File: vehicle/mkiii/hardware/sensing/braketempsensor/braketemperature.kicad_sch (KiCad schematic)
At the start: 15 parts, among them J1 J_PCIe_x1, J2 J_Programming_Pin_Header, U1 MCP2561-E_SN, U2 STM32G441KBT6, Y1 X_16MHz_18pF

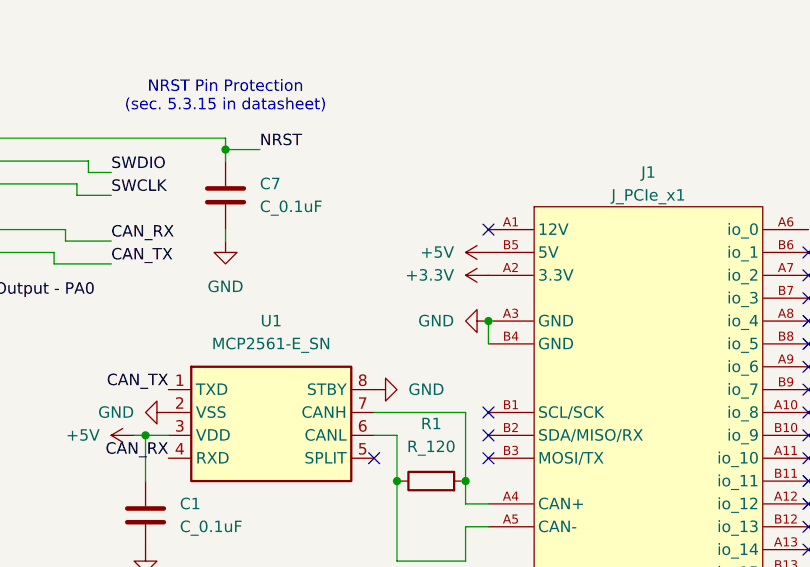
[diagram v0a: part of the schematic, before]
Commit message: first final draft of brake temp sensor, schematic and pcb layout first completion
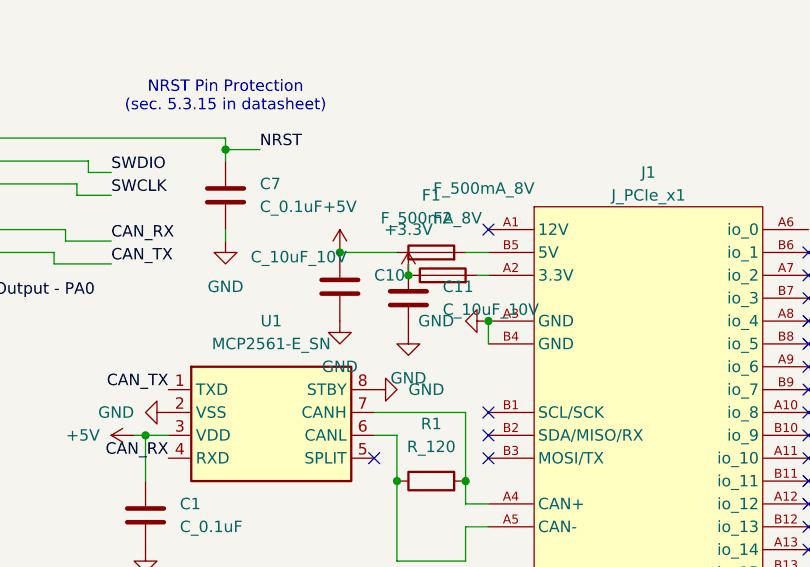
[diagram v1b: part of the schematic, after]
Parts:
- added C10, C11: C_10uF_10V, OEM:C_0603_1608Metric, symbol OEM:C_10uF_10V_0603
- added F1, F2: F_500mA_8V, OEM:Fuse_1206_3216Metric, symbol OEM:F_500mA_8V_1206
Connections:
- net +3.3V: now also C11.1, F2.1; no longer J1.A2 (3.3V)
- net +5V: now also C10.1, F1.1; no longer J1.B5 (5V)
- net GND: now also C10.2, C11.2
- new net: F1.2, J1.B5 (5V)
- new net: F2.2, J1.A2 (3.3V)

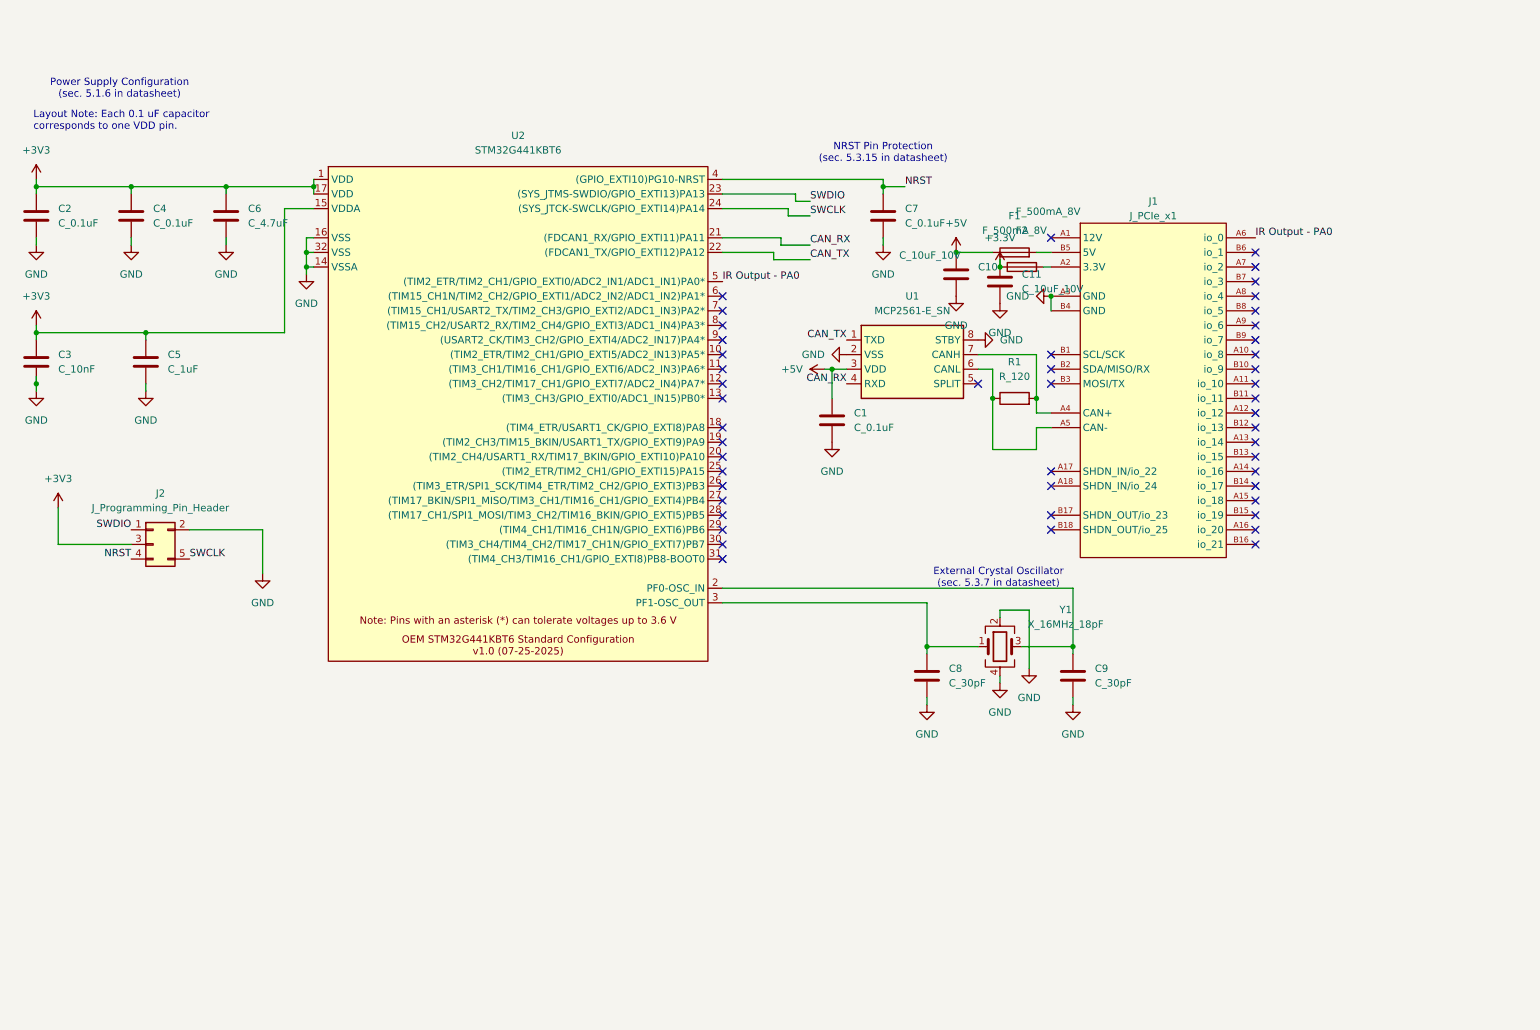
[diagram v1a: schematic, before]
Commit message: Fixed Vias DRC Issues by changing project to OEM Template
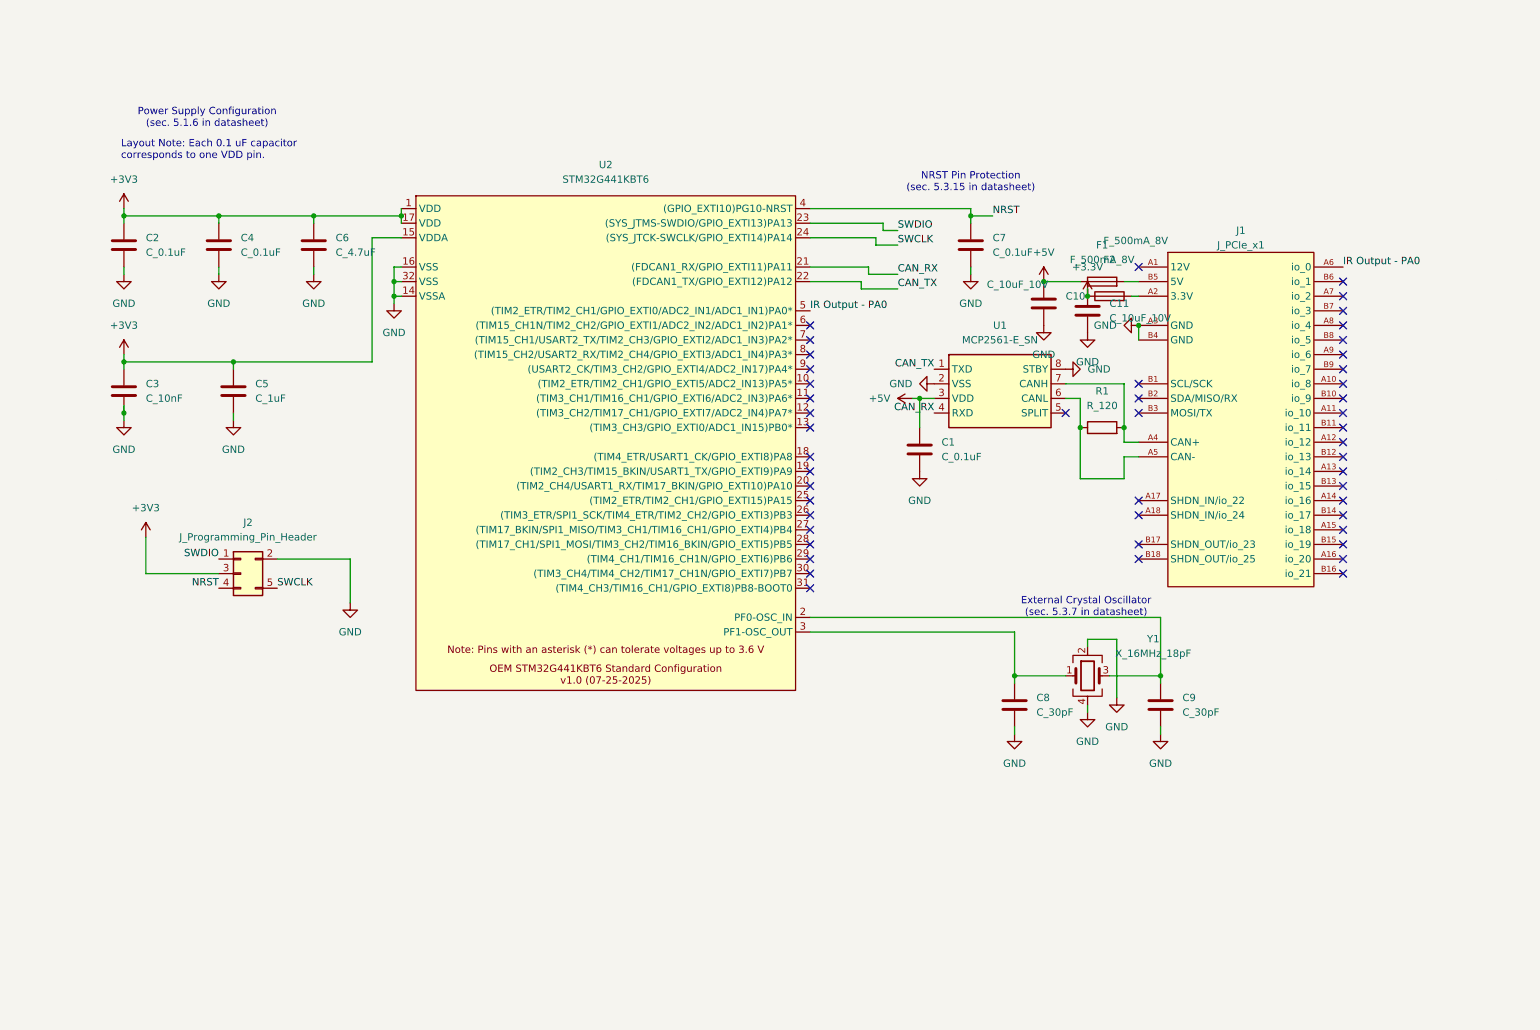
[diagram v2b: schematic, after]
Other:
- title: Brake Temperature Sensor -> (none)
- moved on the sheet: C1, C10, C11, C2, C3, C4, C5, C6, C7, C8, C9, F1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

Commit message: Brake Temp Sensor final version for review
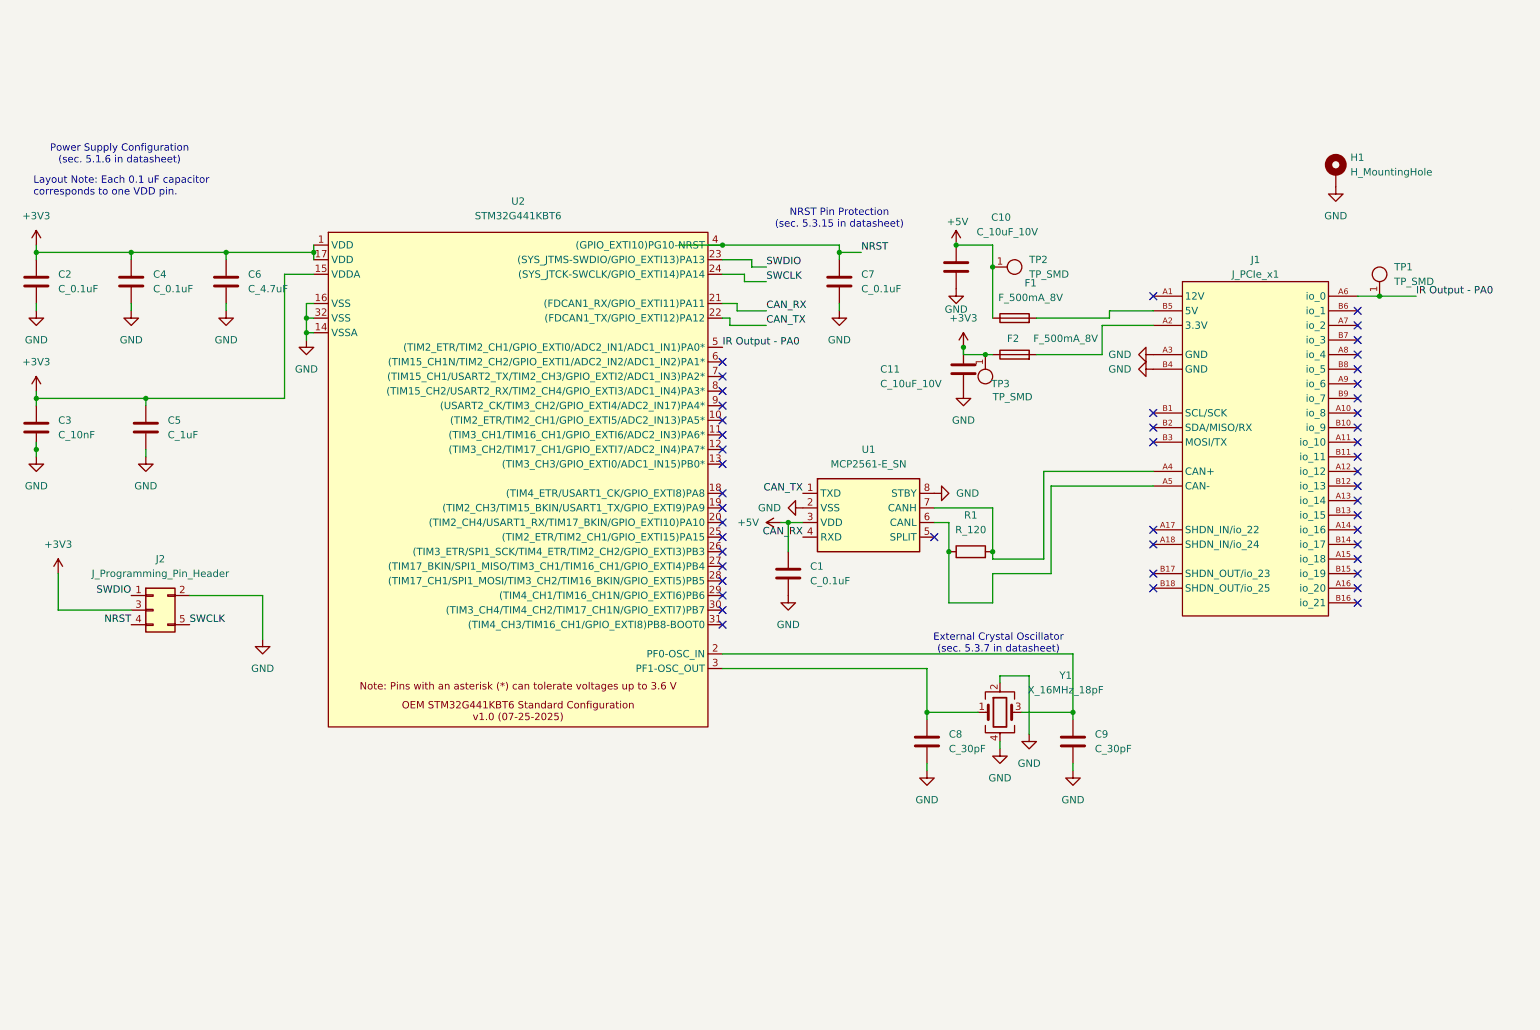
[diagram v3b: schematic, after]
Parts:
- added H1: H_MountingHole, OEM:H_MountingHole, symbol OEM:H_MountingHole
- added TP1, TP2, TP3: TP_SMD, OEM:TP_Hook_SMD, symbol OEM:TP_Hook_SMD
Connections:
- net +3.3V is gone; now on net +3V3: C11.1, F2.1
- net +3V3: now also TP3.1
- net +5V: now also TP2.1
- net GND: now also H1.1
- net IR Output - PA0: now also TP1.1
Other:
- moved on the sheet: C1, C10, C11, C2, C3, C4, C5, C6, C7, C8, C9, F1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

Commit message: Schematics and PCB Layout are Preliminarily Approved - DRC and ERC results are good.
Changes:
- Added Sensor Info to Schematics
- Updated Title Block in Schematics
- Added OEM Logo and Engineer's (Matthew T.) Name
- Moved Mounting Hole to Edge of PCB
- Shrank size of PCB by 4 mm

Good work Matthew :)
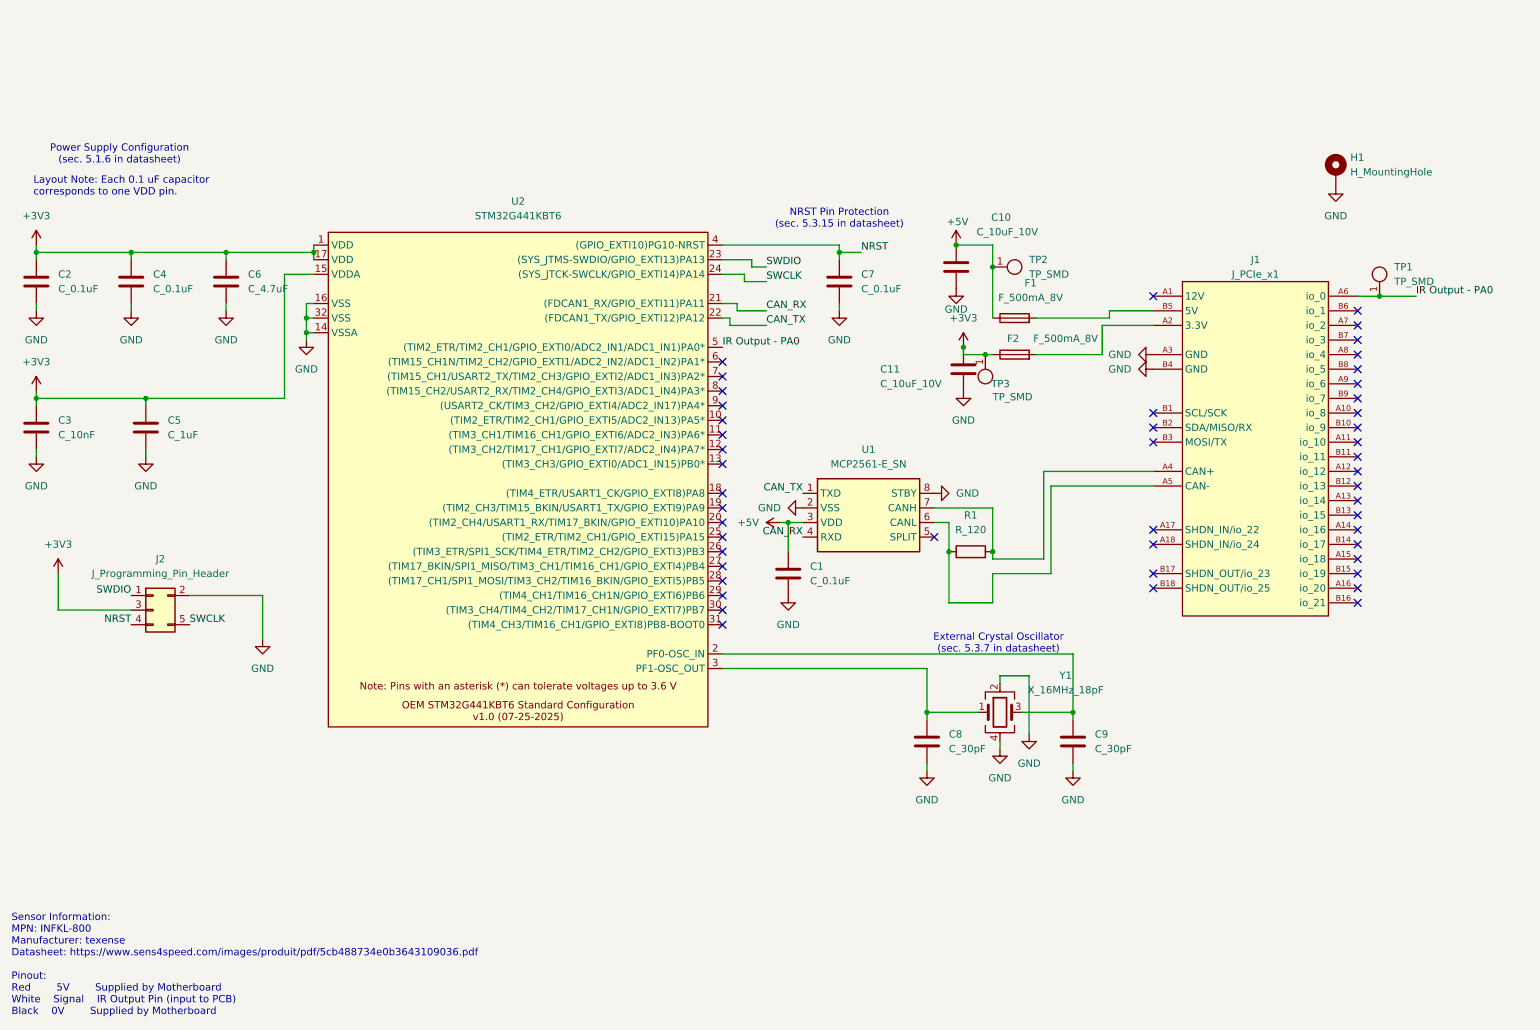
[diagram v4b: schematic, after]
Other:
- note added: "Sensor Information: MPN: INFKL-800 Manufacturer: texense Datasheet: https://www.sens4speed.com/images/produit/pdf/5cb488734e0b3643109036.pdf Pinout: Red 5V Supplied by Motherboard White Signal IR Output Pin (input to PCB) Black 0V Supplied by Motherboard"
- title: (none) -> Brake Temperature Sensor
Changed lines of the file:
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@@
 	(generator_version "9.0")
 	(paper "A4")
+	(title_block
+		(title "Brake Temperature Sensor")
+		(date "2026-01-31")
+		(rev "1.0")
+		(comment 1 "Matthew Townsend")
+	)
 	(text "Power Supply Configuration\n(sec. 5.1.6 in datasheet)"
 		(exclude_from_sim no)
@@
 				(size 1.27 1.27)
 			)
+		)
+	)
+	(text "Sensor Information:\nMPN: INFKL-800\nManufacturer: texense\nDatasheet: https://www.sens4speed.com/images/produit/pdf/5cb488734e0b3643109036.pdf\n\nPinout:\nRed		5V		Supplied by Motherboard\nWhite	Signal	IR Output Pin (input to PCB)\nBlack	0V		Supplied by Motherboard"
+		(exclude_from_sim no)
+		(at 19.812 173.482 0)
+		(effects
+			(font
+				(size 1.27 1.27)
+			)
+			(justify left top)
 		)
 	)
@@
 	)
 	(junction
-		(at 143.51 57.15)
-		(diameter 0)
-		(color 0 0 0 0)
-	)
-	(junction
-		(at 24.13 92.71)
-		(diameter 0)
-		(color 0 0 0 0)
-	)
-	(junction
 		(at 189.23 76.2)
 		(diameter 0)
@@
 	(wire
 		(pts
-			(xy 24.13 91.44) (xy 24.13 92.71)
-		)
-		(stroke
-			(width 0)
-			(type default)
-		)
-	)
-	(wire
-		(pts
 			(xy 50.8 118.11) (xy 63.5 118.11)
 		)
 		(stroke
-			(width 0)
-			(type default)
-		)
-	)
-	(wire
-		(pts
-			(xy 135.89 57.15) (xy 143.51 57.15)
-		)
-		(stroke

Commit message: Brake temperature sensor final version 2/2/26
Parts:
- added D1, D2, D3, D4, D5, D6: D_Red_LED, OEM:D_0805_2012Metric, symbol OEM:D_LED_Red_0805
- added R2, R3, R4, R5, R6, R7: R_1k, OEM:R_0603_1608Metric, symbol OEM:R_1k_0.1W_0603
- added TP4, TP5, TP6: TP_SMD, OEM:TP_Hook_SMD, symbol OEM:TP_Hook_SMD
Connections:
- net +3V3: now also R3.1
- net +5V: now also R2.1
- net GND: now also D1.1 (K), D2.1 (K), D3.1 (K), D4.1 (K), D5.1 (K), D6.1 (K), TP6.1
- net NRST: now also R6.1
- net SWDIO: now also R7.1
- net at J1.A5 (CAN-), R1.1, U1.6 (CANL): now also TP5.1
- net at J1.A4 (CAN+), R1.2, U1.7 (CANH): now also TP4.1
- net Debug LED: now reaches U2.11 ((TIM3_CH1/TIM16_CH1/GPIO_EXTI6/ADC2_IN3)PA6*)
- net Debug LED: now also R5.1
- net Heartbeat LED: now reaches U2.18 ((TIM4_ETR/USART1_CK/GPIO_EXTI8)PA8)
- net Heartbeat LED: now also R4.1
- new net: D6.2 (A), R7.2
- new net: D1.2 (A), R2.2
- new net: D2.2 (A), R3.2
- new net: D3.2 (A), R4.2
- new net: D5.2 (A), R6.2
- new net: D4.2 (A), R5.2
- no-connect marks 48 -> 46
